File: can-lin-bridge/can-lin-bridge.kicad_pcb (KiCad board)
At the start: 2 copper layers, 20 x 24 mm, 24 parts, among them IC1 PIC18F26Q83T-I_5N, J1 ICSP, J2 PWR, J3 CAN, J4 LIN, U1 TJA1029TK/20/1J, U2 TJA1042TK/3/2Z

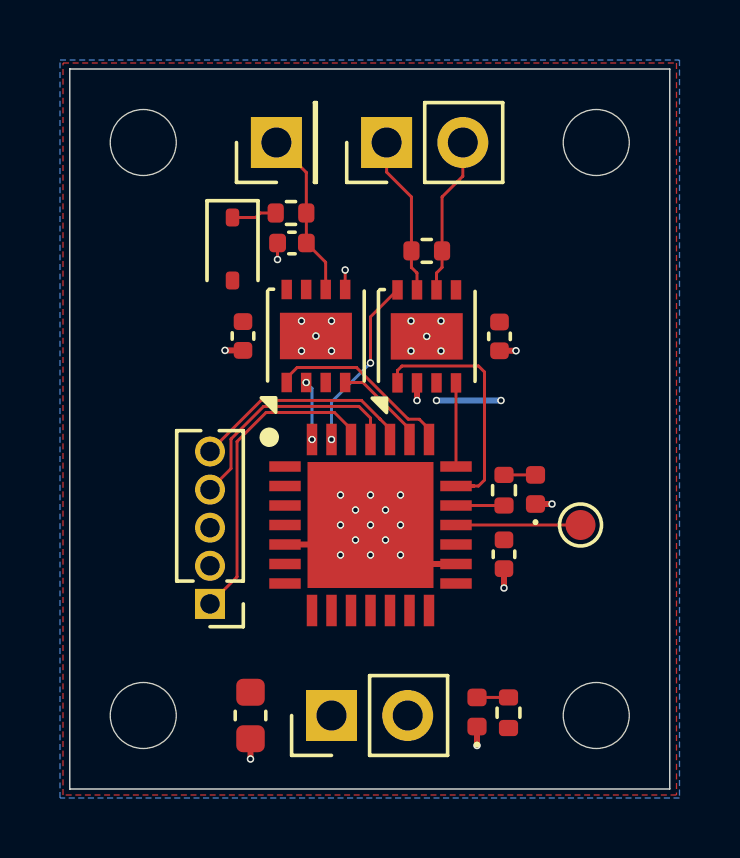
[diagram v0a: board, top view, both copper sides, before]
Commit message: can-lin-bridge: Add silkscreen text to PCB
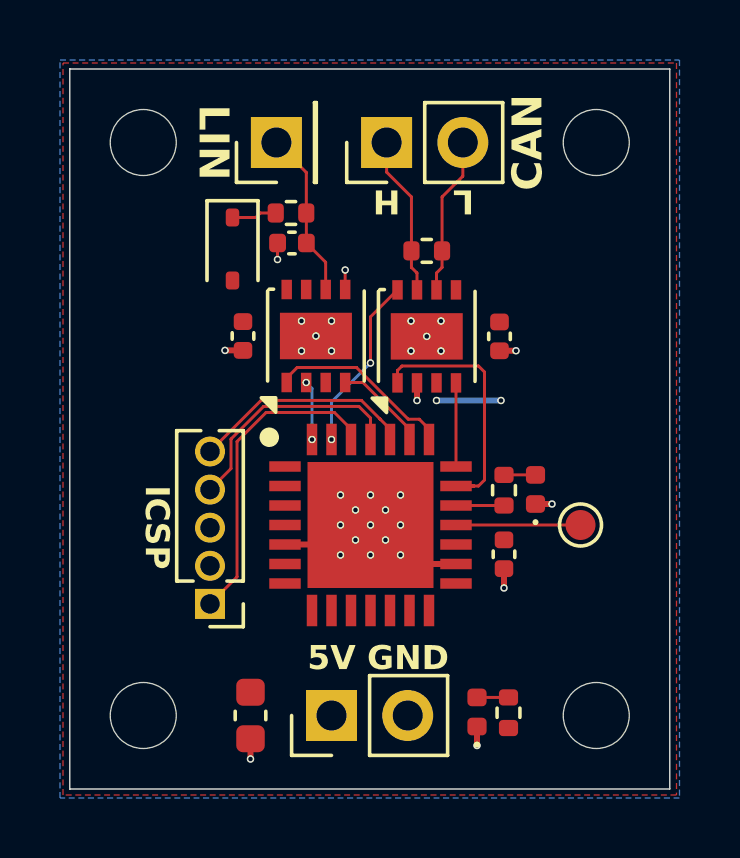
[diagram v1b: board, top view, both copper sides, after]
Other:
- board text added: "5V"
- board text added: "CAN"
- board text added: "GND"
- board text added: "H"
- board text added: "ICSP"
- board text added: "L"
- board text added: "LIN"
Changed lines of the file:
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@@
 		(layer "Edge.Cuts")
+	)
+	(gr_text "GND"
+		(at 146.25 75.9 0)
+		(layer "F.SilkS")
+		(effects
+			(font
+				(size 0.8 0.8)
+				(thickness 0.16)
+				(bold yes)
+			)
+			(justify bottom)
+		)
+	)
+	(gr_text "CAN"
+		(at 149.65 58.25 90)
+		(layer "F.SilkS")
+		(effects
+			(font
+				(size 1 1)
+				(thickness 0.2)
+				(bold yes)
+			)
+			(justify top)
+		)
+	)
+	(gr_text "ICSP"
+		(at 138.35 71.08 270)
+		(layer "F.SilkS")
+		(effects
+			(font
+				(size 0.8 0.8)
+				(thickness 0.16)
+				(bold yes)
+			)
+			(justify top)
+		)
+	)
+	(gr_text "5V"
+		(at 143.70025 75.9 0)
+		(layer "F.SilkS")
+		(effects
+			(font
+				(size 0.8 0.8)
+				(thickness 0.16)
+				(bold yes)
+			)
+			(justify bottom)
+		)
+	)
+	(gr_text "LIN"
+		(at 140.35 58.25 270)
+		(layer "F.SilkS")
+		(effects
+			(font
+				(size 1 1)
+				(thickness 0.2)
+				(bold yes)
+			)
+			(justify top)
+		)
+	)
+	(gr_text "L"
+		(at 148.1 59.75 180)
+		(layer "F.SilkS")
+		(effects
+			(font
+				(size 0.8 0.8)
+				(thickness 0.16)
+				(bold yes)
+			)
+			(justify bottom)
+		)
+	)
+	(gr_text "H"
+		(at 145.53775 59.75 180)
+		(layer "F.SilkS")
+		(effects
+			(font
+				(size 0.8 0.8)
+				(thickness 0.16)
+				(bold yes)
+			)
+			(justify bottom)
+		)
+	)
+	(dimension
+		(type orthogonal)
+		(layer "F.Fab")
+		(pts
+			(xy 152.52525 58.25) (xy 152.52525 77.35)
+		)
+		(height 5.02475)
+		(orientation 1)
+		(format
+			(prefix "")
+			(suffix "")
+			(units 3)
+			(units_format 0)
+			(precision 4)
+			(suppress_zeroes yes)
+		)
+		(style
+			(thickness 0.1)
+			(arrow_length 1.27)
+			(text_position_mode 0)
+			(arrow_direction outward)
+			(extension_height 0.58642)
+			(extension_offset 0.5)
+			(keep_text_aligned yes)
+		)
+		(gr_text "19.1"
+			(at 156.4 67.8 90)
+			(layer "F.Fab")
+			(effects
+				(font
+					(size 1 1)
+					(thickness 0.15)
+				)
+			)
+		)
+	)
+	(dimension
+		(type orthogonal)
+		(layer "F.Fab")
+		(pts
+			(xy 154.97525 55.8) (xy 154.97525 79.8)
+		)
+		(height 5.42475)
+		(orientation 1)
+		(format
+			(prefix "")
+			(suffix "")
+			(units 3)
+			(units_format 0)
+			(precision 4)
+			(suppress_zeroes yes)
+		)
+		(style
+			(thickness 0.1)
+			(arrow_length 1.27)
+			(text_position_mode 0)
+			(arrow_direction outward)
+			(extension_height 0.58642)
+			(extension_offset 0.5)
+			(keep_text_aligned yes)
+		)
+		(gr_text "24"
+			(at 159.25 67.8 90)
+			(layer "F.Fab")
+			(effects
+				(font
+					(size 1 1)
+					(thickness 0.15)
+				)
+			)
+		)
+	)
+	(dimension
+		(type orthogonal)
+		(layer "F.Fab")
+		(pts
+			(xy 134.97525 55.8) (xy 154.97525 55.8)
+		)
+		(height -4.75)
+		(orientation 0)
+		(format
+			(prefix "")
+			(suffix "")
+			(units 3)
+			(units_format 0)
+			(precision 4)
+			(suppress_zeroes yes)
+		)
+		(style
+			(thickness 0.1)
+			(arrow_length 1.27)
+			(text_position_mode 0)
+			(arrow_direction outward)
+			(extension_height 0.58642)
+			(extension_offset 0.5)
+			(keep_text_aligned yes)
+		)
+		(gr_text "20"
+			(at 144.97525 49.9 0)
+			(layer "F.Fab")
+			(effects
+				(font
+					(size 1 1)
+					(thickness 0.15)
+				)
+			)
+		)
+	)
+	(dimension
+		(type orthogonal)
+		(layer "F.Fab")
+		(pts
+			(xy 137.42525 58.25) (xy 152.52525 58.25)
+		)
+		(height -4.3)
+		(orientation 0)
+		(format
+			(prefix "")
+			(suffix "")
+			(units 3)
+			(units_format 0)
+			(precision 4)
+			(suppress_zeroes yes)
+		)
+		(style
+			(thickness 0.1)
+			(arrow_length 1.27)
+			(text_position_mode 0)
+			(arrow_direction outward)
+			(extension_height 0.58642)
+			(extension_offset 0.5)
+			(keep_text_aligned yes)
+		)
+		(gr_text "15.1"
+			(at 144.97525 52.8 0)
+			(layer "F.Fab")
+			(effects
+				(font
+					(size 1 1)
+					(thickness 0.15)
+				)
+			)
+		)
 	)
 	(segment
